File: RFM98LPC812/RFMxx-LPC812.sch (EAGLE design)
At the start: 21 parts, among them X1 BU-SMA-V, X2 BU-SMA-V

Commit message: no comment
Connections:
- new net N$25: U$1.PIO0_7, U$2.RESET, U$3.RESET
- net N$17: now also U$2.DIO4
- net N$18: now also U$2.DIO5
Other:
- moved on the sheet: LED1, LED2, LED3, LED4, LED5, LED6, R1, R2, R3, R4, R5, R6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
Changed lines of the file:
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@@
 <instances>
 <instance part="U$2" gate="G$1" x="0" y="2.54"/>
-<instance part="X1" gate="G$1" x="33.02" y="-2.54" rot="R180"/>
+<instance part="X1" gate="G$1" x="20.32" y="-10.16" rot="R180"/>
 <instance part="X2" gate="G$1" x="30.48" y="25.4" rot="R180"/>
 <instance part="JP1" gate="A" x="-43.18" y="40.64"/>
 <instance part="U$1" gate="G$1" x="-93.98" y="45.72"/>
 <instance part="U$3" gate="G$1" x="0" y="38.1"/>
-<instance part="R1" gate="G$1" x="48.26" y="10.16" rot="R90"/>
-<instance part="R2" gate="G$1" x="58.42" y="10.16" rot="R90"/>
-<instance part="R3" gate="G$1" x="68.58" y="10.16" rot="R90"/>
-<instance part="R4" gate="G$1" x="78.74" y="10.16" rot="R90"/>
-<instance part="R5" gate="G$1" x="88.9" y="10.16" rot="R90"/>
-<instance part="R6" gate="G$1" x="99.06" y="10.16" rot="R90"/>
-<instance part="LED1" gate="G$1" x="48.26" y="20.32"/>
-<instance part="LED2" gate="G$1" x="58.42" y="20.32"/>
-<instance part="LED3" gate="G$1" x="68.58" y="20.32"/>
-<instance part="LED4" gate="G$1" x="78.74" y="20.32"/>
-<instance part="LED5" gate="G$1" x="88.9" y="20.32"/>
-<instance part="LED6" gate="G$1" x="99.06" y="20.32"/>
+<instance part="R1" gate="G$1" x="55.88" y="10.16" rot="R90"/>
+<instance part="R2" gate="G$1" x="66.04" y="10.16" rot="R90"/>
+<instance part="R3" gate="G$1" x="76.2" y="10.16" rot="R90"/>
+<instance part="R4" gate="G$1" x="86.36" y="10.16" rot="R90"/>
+<instance part="R5" gate="G$1" x="96.52" y="10.16" rot="R90"/>
+<instance part="R6" gate="G$1" x="106.68" y="10.16" rot="R90"/>
+<instance part="LED1" gate="G$1" x="55.88" y="20.32"/>
+<instance part="LED2" gate="G$1" x="66.04" y="20.32"/>
+<instance part="LED3" gate="G$1" x="76.2" y="20.32"/>
+<instance part="LED4" gate="G$1" x="86.36" y="20.32"/>
+<instance part="LED5" gate="G$1" x="96.52" y="20.32"/>
+<instance part="LED6" gate="G$1" x="106.68" y="20.32"/>
 <instance part="JP2" gate="A" x="-142.24" y="81.28" rot="R180"/>
 <instance part="JP3" gate="A" x="-144.78" y="50.8" rot="R180"/>
@@
 <instance part="GND2" gate="1" x="-101.6" y="68.58" rot="R180"/>
 <instance part="GND3" gate="1" x="27.94" y="30.48" rot="R180"/>
-<instance part="GND4" gate="1" x="30.48" y="2.54" rot="R180"/>
-<instance part="GND5" gate="1" x="48.26" y="2.54"/>
-<instance part="GND6" gate="1" x="58.42" y="2.54"/>
-<instance part="GND7" gate="1" x="68.58" y="2.54"/>
-<instance part="GND8" gate="1" x="78.74" y="2.54"/>
-<instance part="GND9" gate="1" x="88.9" y="2.54"/>
-<instance part="GND10" gate="1" x="99.06" y="2.54"/>
+<instance part="GND4" gate="1" x="27.94" y="-5.08" rot="R180"/>
+<instance part="GND5" gate="1" x="55.88" y="2.54"/>
+<instance part="GND6" gate="1" x="66.04" y="2.54"/>
+<instance part="GND7" gate="1" x="76.2" y="2.54"/>
+<instance part="GND8" gate="1" x="86.36" y="2.54"/>
+<instance part="GND9" gate="1" x="96.52" y="2.54"/>
+<instance part="GND10" gate="1" x="106.68" y="2.54"/>
 <instance part="GND11" gate="1" x="-17.78" y="-5.08"/>
 <instance part="GND12" gate="1" x="-17.78" y="27.94"/>
@@
 <pinref part="U$2" gate="G$1" pin="ANT"/>
 <pinref part="X1" gate="G$1" pin="1"/>
-<wire x1="17.78" y1="-2.54" x2="30.48" y2="-2.54" width="0.1524" layer="91"/>
+<wire x1="17.78" y1="-2.54" x2="17.78" y2="-10.16" width="0.1524" layer="91"/>
 </segment>
 </net>
@@
 <pinref part="LED6" gate="G$1" pin="A"/>
 <wire x1="17.78" y1="45.72" x2="35.56" y2="45.72" width="0.1524" layer="91"/>
-<wire x1="35.56" y1="45.72" x2="99.06" y2="45.72" width="0.1524" layer="91"/>
-<wire x1="99.06" y1="45.72" x2="99.06" y2="22.86" width="0.1524" layer="91"/>
+<wire x1="35.56" y1="45.72" x2="106.68" y2="45.72" width="0.1524" layer="91"/>
+<wire x1="106.68" y1="45.72" x2="106.68" y2="22.86" width="0.1524" layer="91"/>
 <pinref part="U$2" gate="G$1" pin="DIO0"/>
 <wire x1="17.78" y1="12.7" x2="35.56" y2="12.7" width="0.1524" layer="91"/>
@@
 <pinref part="LED5" gate="G$1" pin="A"/>
 <wire x1="17.78" y1="43.18" x2="38.1" y2="43.18" width="0.1524" layer="91"/>
-<wire x1="38.1" y1="43.18" x2="88.9" y2="43.18" width="0.1524" layer="91"/>
-<wire x1="88.9" y1="43.18" x2="88.9" y2="22.86" width="0.1524" layer="91"/>
+<wire x1="38.1" y1="43.18" x2="96.52" y2="43.18" width="0.1524" layer="91"/>
+<wire x1="96.52" y1="43.18" x2="96.52" y2="22.86" width="0.1524" layer="91"/>
 <pinref part="U$2" gate="G$1" pin="DIO1"/>
 <wire x1="17.78" y1="10.16" x2="38.1" y2="10.16" width="0.1524" layer="91"/>
@@
 <pinref part="LED4" gate="G$1" pin="A"/>
 <wire x1="17.78" y1="40.64" x2="40.64" y2="40.64" width="0.1524" layer="91"/>
-<wire x1="40.64" y1="40.64" x2="78.74" y2="40.64" width="0.1524" layer="91"/>
-<wire x1="78.74" y1="40.64" x2="78.74" y2="22.86" width="0.1524" layer="91"/>
+<wire x1="40.64" y1="40.64" x2="86.36" y2="40.64" width="0.1524" layer="91"/>
+<wire x1="86.36" y1="40.64" x2="86.36" y2="22.86" width="0.1524" layer="91"/>
 <pinref part="U$2" gate="G$1" pin="DIO2"/>
 <wire x1="17.78" y1="7.62" x2="40.64" y2="7.62" width="0.1524" layer="91"/>
@@
 <pinref part="LED3" gate="G$1" pin="A"/>
 <wire x1="17.78" y1="38.1" x2="43.18" y2="38.1" width="0.1524" layer="91"/>
-<wire x1="43.18" y1="38.1" x2="68.58" y2="38.1" width="0.1524" layer="91"/>
-<wire x1="68.58" y1="38.1" x2="68.58" y2="22.86" width="0.1524" layer="91"/>
+<wire x1="43.18" y1="38.1" x2="76.2" y2="38.1" width="0.1524" layer="91"/>
+<wire x1="76.2" y1="38.1" x2="76.2" y2="22.86" width="0.1524" layer="91"/>
 <pinref part="U$2" gate="G$1" pin="DIO3"/>
 <wire x1="17.78" y1="5.08" x2="43.18" y2="5.08" width="0.1524" layer="91"/>
@@
 <pinref part="U$3" gate="G$1" pin="DIO4"/>
 <pinref part="LED2" gate="G$1" pin="A"/>
-<wire x1="17.78" y1="35.56" x2="58.42" y2="35.56" width="0.1524" layer="91"/>
-<wire x1="58.42" y1="35.56" x2="58.42" y2="22.86" width="0.1524" layer="91"/>
+<wire x1="17.78" y1="35.56" x2="45.72" y2="35.56" width="0.1524" layer="91"/>
+<wire x1="45.72" y1="35.56" x2="66.04" y2="35.56" width="0.1524" layer="91"/>
+<wire x1="66.04" y1="35.56" x2="66.04" y2="22.86" width="0.1524" layer="91"/>
+<pinref part="U$2" gate="G$1" pin="DIO4"/>
+<wire x1="17.78" y1="2.54" x2="45.72" y2="2.54" width="0.1524" layer="91"/>
+<wire x1="45.72" y1="2.54" x2="45.72" y2="35.56" width="0.1524" layer="91"/>
+<junction x="45.72" y="35.56"/>
 </segment>
 </net>
@@
 <pinref part="LED1" gate="G$1" pin="A"/>
 <wire x1="17.78" y1="33.02" x2="48.26" y2="33.02" width="0.1524" layer="91"/>
-<wire x1="48.26" y1="33.02" x2="48.26" y2="22.86" width="0.1524" layer="91"/>
+<wire x1="48.26" y1="33.02" x2="55.88" y2="33.02" width="0.1524" layer="91"/>
+<wire x1="55.88" y1="33.02" x2="55.88" y2="22.86" width="0.1524" layer="91"/>
+<pinref part="U$2" gate="G$1" pin="DIO5"/>
+<wire x1="17.78" y1="0" x2="48.26" y2="0" width="0.1524" layer="91"/>
+<wire x1="48.26" y1="0" x2="48.26" y2="33.02" width="0.1524" layer="91"/>
+<junction x="48.26" y="33.02"/>
 </segment>
 </net>
@@
 <pinref part="X1" gate="G$1" pin="2"/>
 <pinref part="GND4" gate="1" pin="GND"/>
+<wire x1="17.78" y1="-7.62" x2="27.94" y2="-7.62" width="0.1524" layer="91"/>
 </segment>
 <segment>
@@
 </segment>
 </net>
+<net name="N$25" class="0">
+<segment>
+<pinref part="U$1" gate="G$1" pin="PIO0_7"/>
+<wire x1="-60.96" y1="50.8" x2="-53.34" y2="50.8" width="0.1524" layer="91"/>
+<wire x1="-53.34" y1="50.8" x2="-53.34" y2="27.94" width="0.1524" layer="91"/>
+<pinref part="U$2" gate="G$1" pin="RESET"/>
+<wire x1="-53.34" y1="27.94" x2="-53.34" y2="0" width="0.1524" layer="91"/>
+<wire x1="-53.34" y1="0" x2="-17.78" y2="0" width="0.1524" layer="91"/>
+<wire x1="-53.34" y1="27.94" x2="-22.86" y2="27.94" width="0.1524" layer="91"/>
+<wire x1="-22.86" y1="27.94" x2="-22.86" y2="33.02" width="0.1524" layer="91"/>
+<pinref part="U$3" gate="G$1" pin="RESET"/>
+<wire x1="-22.86" y1="33.02" x2="-17.78" y2="33.02" width="0.1524" layer="91"/>
+<junction x="-53.34" y="27.94"/>
+</segment>
+</net>

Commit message: no comment
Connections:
- new net N$26: R1.1, R2.1, R3.1, R4.1, R5.1, R6.1, U$1.VSS, U$2.GND, U$2.GND@2, U$2.GND@3, U$3.GND, U$4.-, X2.2
- net GND: no longer R1.1, R2.1, R3.1, R4.1, R5.1, R6.1, U$1.VSS, U$2.GND, U$3.GND, U$4.-, X2.2
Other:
- moved on the sheet: X1
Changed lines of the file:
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@@
 <part name="P+3" library="supply1" deviceset="VCC" device=""/>
 <part name="P+4" library="supply1" deviceset="VCC" device=""/>
+<part name="GND13" library="supply1" deviceset="GND" device=""/>
+<part name="GND14" library="supply1" deviceset="GND" device=""/>
 </parts>
 <sheets>
@@
 <instances>
 <instance part="U$2" gate="G$1" x="0" y="2.54"/>
-<instance part="X1" gate="G$1" x="20.32" y="-10.16" rot="R180"/>
+<instance part="X1" gate="G$1" x="33.02" y="-12.7" rot="R180"/>
 <instance part="X2" gate="G$1" x="30.48" y="25.4" rot="R180"/>
 <instance part="JP1" gate="A" x="-43.18" y="40.64"/>
@@
 <instance part="GND2" gate="1" x="-101.6" y="68.58" rot="R180"/>
 <instance part="GND3" gate="1" x="27.94" y="30.48" rot="R180"/>
-<instance part="GND4" gate="1" x="27.94" y="-5.08" rot="R180"/>
+<instance part="GND4" gate="1" x="30.48" y="-7.62" rot="R180"/>
 <instance part="GND5" gate="1" x="55.88" y="2.54"/>
 <instance part="GND6" gate="1" x="66.04" y="2.54"/>
@@
 <instance part="P+3" gate="VCC" x="-17.78" y="48.26"/>
 <instance part="P+4" gate="VCC" x="-17.78" y="15.24"/>
+<instance part="GND13" gate="1" x="-2.54" y="-12.7"/>
+<instance part="GND14" gate="1" x="2.54" y="-12.7"/>
 </instances>
 <busses>
@@
 <wire x1="17.78" y1="30.48" x2="27.94" y2="25.4" width="0.1524" layer="91"/>
 <pinref part="U$3" gate="G$1" pin="ANT"/>
-</segment>
-</net>
-<net name="N$6" class="0">
-<segment>
-<pinref part="U$2" gate="G$1" pin="ANT"/>
-<pinref part="X1" gate="G$1" pin="1"/>
-<wire x1="17.78" y1="-2.54" x2="17.78" y2="-10.16" width="0.1524" layer="91"/>
 </segment>
 </net>
@@
 </segment>
 </net>
-<net name="GND" class="0">
+<net name="N$26" class="0">
 <segment>
 <pinref part="U$4" gate="G$1" pin="-"/>
@@
 </segment>
 <segment>
-<pinref part="X1" gate="G$1" pin="2"/>
-<pinref part="GND4" gate="1" pin="GND"/>
-<wire x1="17.78" y1="-7.62" x2="27.94" y2="-7.62" width="0.1524" layer="91"/>
-</segment>
-<segment>
 <pinref part="R1" gate="G$1" pin="1"/>
 <pinref part="GND5" gate="1" pin="GND"/>
@@
 <pinref part="U$3" gate="G$1" pin="GND"/>
 <pinref part="GND12" gate="1" pin="GND"/>
+</segment>
+<segment>
+<pinref part="U$2" gate="G$1" pin="GND@2"/>
+<pinref part="GND13" gate="1" pin="GND"/>
+</segment>
+<segment>
+<pinref part="U$2" gate="G$1" pin="GND@3"/>
+<pinref part="GND14" gate="1" pin="GND"/>
 </segment>
 </net>
@@
 </segment>
 </net>
+<net name="GND" class="0">
+<segment>
+<pinref part="X1" gate="G$1" pin="2"/>
+<pinref part="GND4" gate="1" pin="GND"/>
+</segment>
+</net>
+<net name="N$6" class="0">
+<segment>
+<pinref part="U$2" gate="G$1" pin="ANT"/>
+<wire x1="17.78" y1="-2.54" x2="20.32" y2="-2.54" width="0.1524" layer="91"/>
+<wire x1="20.32" y1="-2.54" x2="20.32" y2="-12.7" width="0.1524" layer="91"/>
+<pinref part="X1" gate="G$1" pin="1"/>
+<wire x1="20.32" y1="-12.7" x2="30.48" y2="-12.7" width="0.1524" layer="91"/>
+</segment>
+</net>

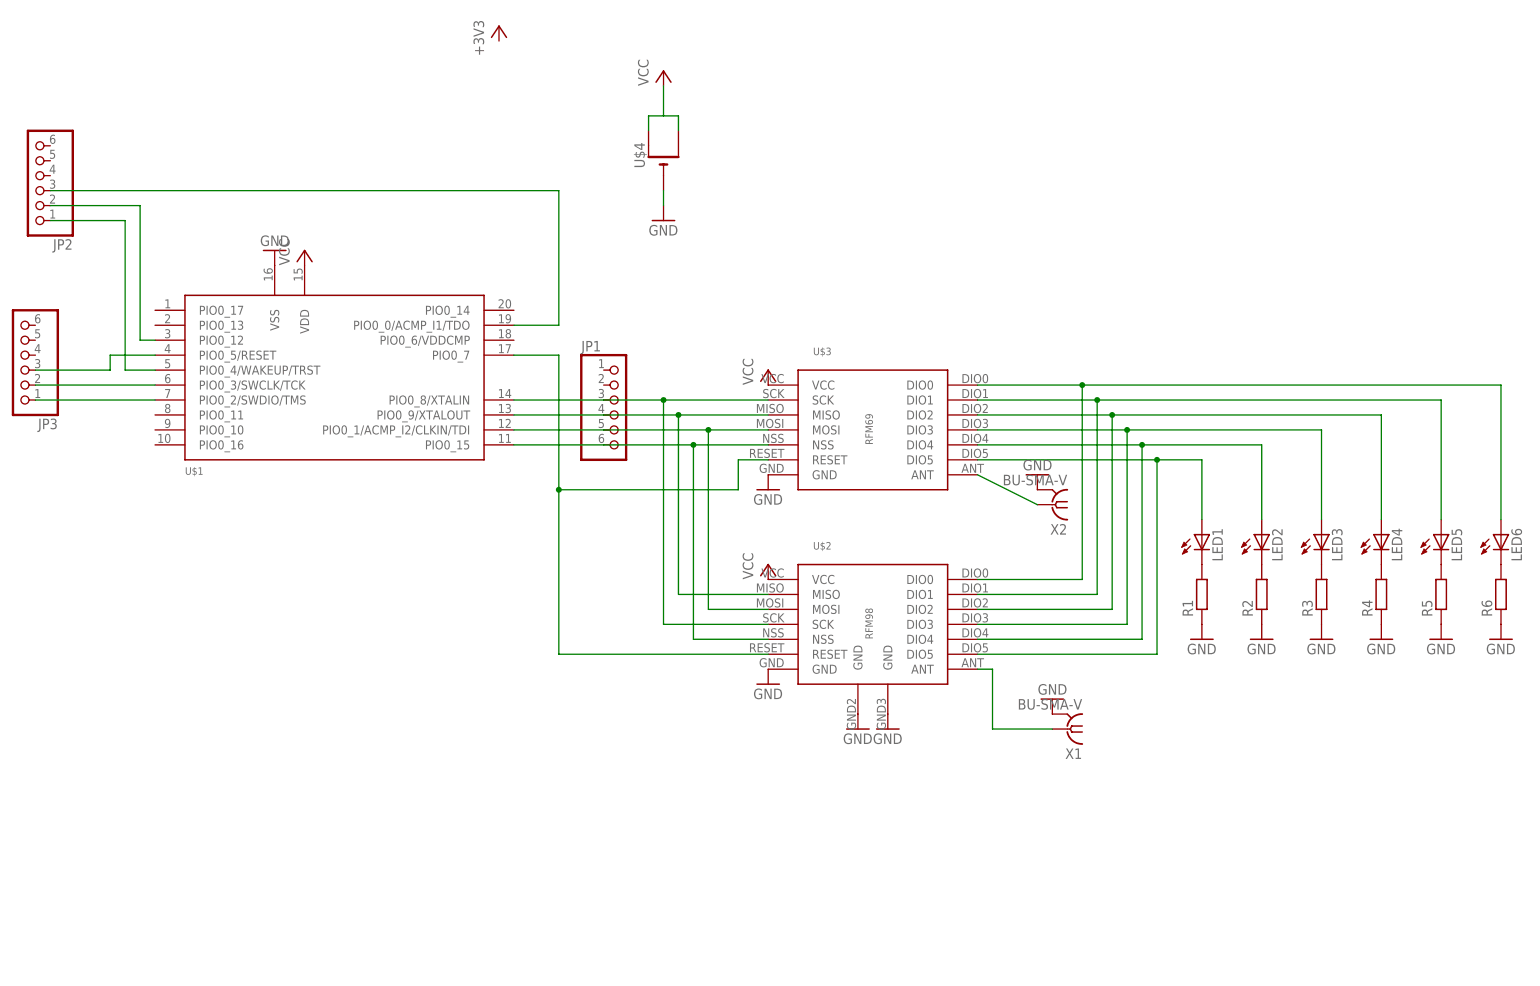
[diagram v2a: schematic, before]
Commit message: reasonably good layout on RFM98 side
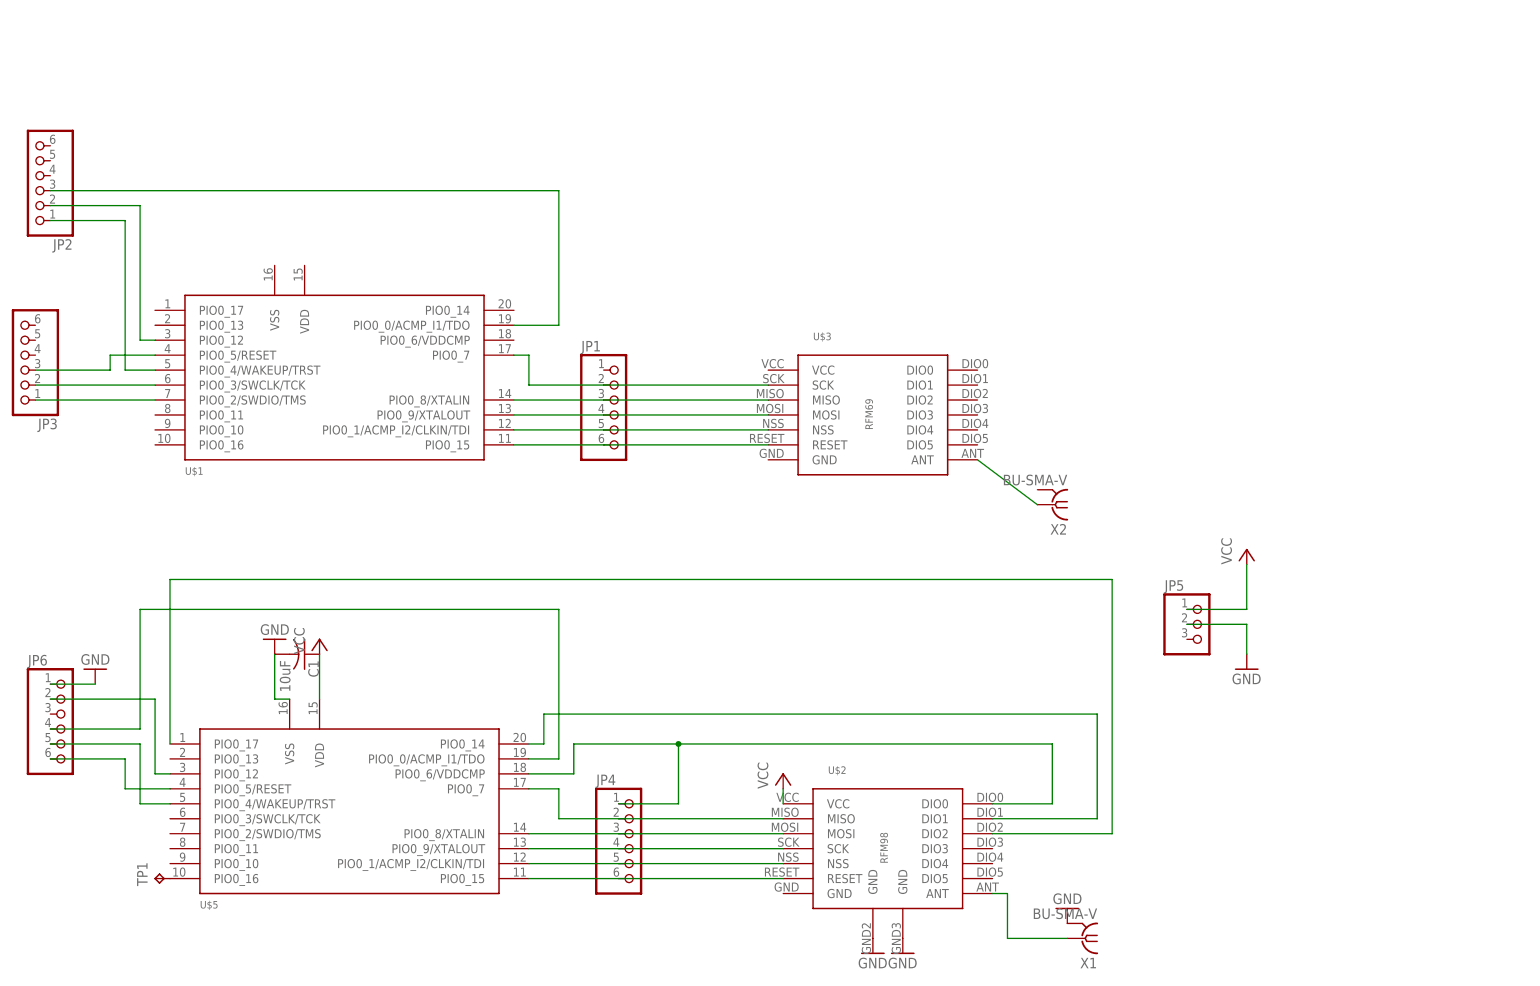
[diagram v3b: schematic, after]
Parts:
- removed LED1, LED2, LED3, LED4, LED5, LED6: (no value), adafruit:LEDSMT1206
- removed R1, R2, R3, R4, R5, R6: (no value), resistor:R-EU_M0805
- removed U$4: (no value), adafruit:CR1220SMT
- added C1: 10uF, adafruit:C-USC0805
- added JP4, JP6: (no value), adafruit:PINHD-1X6
- added JP5: (no value), adafruit:PINHD-1X3
- added TP1: TPB1,27, testpad:TPB1,27
- added U$5: LPC812M101JD20, LPC812:LPC812M101JD20
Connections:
- removed net N$7: LED1.C, R1.2
- new net N$27: U$2.DIO1, U$5.PIO0_14
- net GND: now also C1.2, JP5.2, JP6.1, U$2.GND@2, U$2.GND@3, U$5.VSS
- net N$10: now also JP4.4, U$2.SCK, U$5.PIO0_9/XTALOUT; no longer LED4.C, R4.2
- net N$11: now also JP4.2, U$2.MISO, U$5.PIO0_7; no longer LED5.C, R5.2
- net N$12: now also JP4.6, U$2.RESET, U$5.PIO0_15; no longer LED6.C, R6.2
- net N$13: now also JP1.6, U$1.PIO0_15, U$3.RESET; no longer LED6.A, U$2.DIO0, U$3.DIO0
- net N$14: now also JP1.5, U$1.PIO0_1/ACMP_I2/CLKIN/TDI, U$3.NSS; no longer LED5.A, U$2.DIO1, U$3.DIO1
- net N$15: now also JP1.4, U$1.PIO0_9/XTALOUT, U$3.MOSI; no longer LED4.A, U$2.DIO2, U$3.DIO2
- net N$16: now also JP1.3, U$1.PIO0_8/XTALIN, U$3.MISO; no longer LED3.A, U$2.DIO3, U$3.DIO3
- net N$17: now also JP6.6, U$5.PIO0_5/RESET; no longer LED2.A, U$2.DIO4, U$3.DIO4
- net N$18: now also JP6.5, U$5.PIO0_4/WAKEUP/TRST; no longer LED1.A, U$2.DIO5, U$3.DIO5
- net N$19: now also JP1.2, U$1.PIO0_7, U$3.SCK; no longer JP1.5, U$1.PIO0_1/ACMP_I2/CLKIN/TDI, U$2.MOSI, U$3.MOSI
- net N$20: now also JP6.4, U$5.PIO0_0/ACMP_I1/TDO; no longer JP1.6, U$1.PIO0_15, U$2.NSS, U$3.NSS
- net N$21: now also JP6.2, U$5.PIO0_12; no longer JP1.3, U$1.PIO0_8/XTALIN, U$2.SCK, U$3.SCK
- net N$22: now also JP4.1, U$2.DIO0, U$5.PIO0_6/VDDCMP; no longer JP1.4, U$1.PIO0_9/XTALOUT, U$2.MISO, U$3.MISO
- net N$25: now also TP1.TP, U$5.PIO0_16; no longer U$1.PIO0_7, U$2.RESET, U$3.RESET
- net N$26: now also U$2.DIO2, U$5.PIO0_17; no longer R1.1, R2.1, R3.1, R4.1, R5.1, R6.1, U$1.VSS, U$2.GND, U$2.GND@2, U$2.GND@3, U$3.GND, U$4.-, X2.2
- net N$8: now also JP4.5, U$2.NSS, U$5.PIO0_1/ACMP_I2/CLKIN/TDI; no longer LED2.C, R2.2
- net N$9: now also JP4.3, U$2.MOSI, U$5.PIO0_8/XTALIN; no longer LED3.C, R3.2
- net VCC: now also C1.1, JP5.1, U$5.VDD; no longer U$1.VDD, U$3.VCC, U$4.+, U$4.+1
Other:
- moved on the sheet: U$2, U$3, X1
